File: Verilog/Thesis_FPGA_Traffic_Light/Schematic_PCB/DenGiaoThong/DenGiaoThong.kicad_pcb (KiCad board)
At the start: 2 copper layers, 33 parts, among them J1 Conn_01x10_Male, Q1 2SC1815, Q2 2SC1815, Q3 2SC1815, Q4 2SC1815, Q5 2SC1815, Q6 2SC1815, Q7 2SC1815, Q8 2SC1815

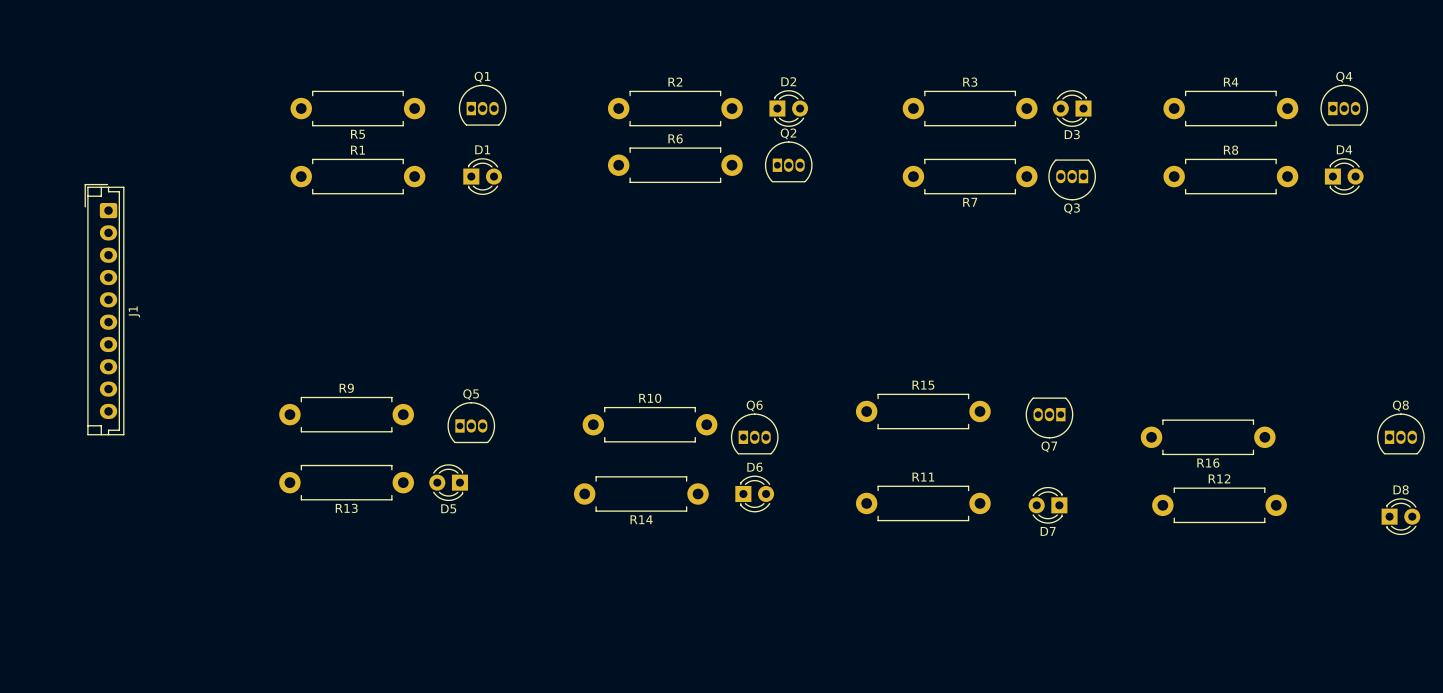
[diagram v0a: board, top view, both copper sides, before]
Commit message: update test git ignore
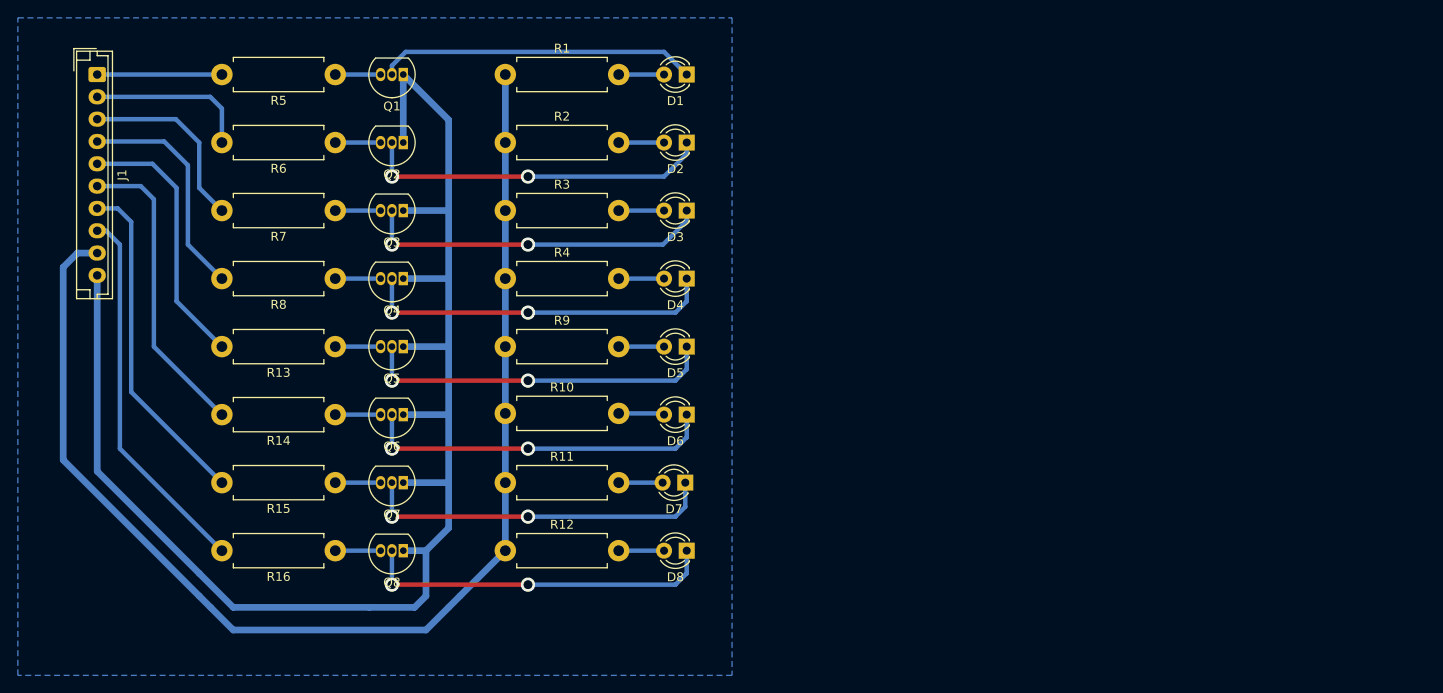
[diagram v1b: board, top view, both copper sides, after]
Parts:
- moved Q8 111.2 mm to (68.6, 80.0), turned to 180 degrees
- moved Q4 105.9 mm to (68.6, 49.5), turned to 180 degrees
- moved R16 104.9 mm to (61.0, 80.0)
- moved R8 94.7 mm to (61.0, 49.5), turned to 180 degrees
- moved D8 78.8 mm to (100.3, 80.0), turned to 180 degrees
- moved R7 77.6 mm to (61.0, 41.9)
- moved R4 77.3 mm to (80.0, 49.5)
- moved Q3 76.3 mm to (68.6, 41.9)
- moved Q7 74.1 mm to (68.6, 72.4)
- moved R12 73.8 mm to (80.0, 80.0)
- moved D4 73.3 mm to (100.3, 49.5), turned to 180 degrees
- moved R15 60.1 mm to (61.0, 72.4), turned to 180 degrees
- moved R3 47.1 mm to (80.0, 41.9)
- moved D3 45.9 mm to (100.3, 41.9)
- moved D7 42.0 mm to (100.2, 72.4)
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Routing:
- net GNDREF: track 0.00 -> 162.2 mm
- net /5V: track 0.00 -> 140.5 mm
- net /SB_PL: track 0.00 -> 42.2 mm
- net Net-(D6-Pad1): track 0.00 -> 39.9 mm, vias 0 -> 2
- net Net-(D5-Pad1): track 0.00 -> 39.9 mm, vias 0 -> 2
- net Net-(D4-Pad1): track 0.00 -> 39.9 mm, vias 0 -> 2
- net Net-(D8-Pad1): track 0.00 -> 39.9 mm, vias 0 -> 2
- net Net-(D7-Pad1): track 0.00 -> 39.8 mm, vias 0 -> 2
- net Net-(D2-Pad1): track 0.00 -> 39.2 mm, vias 0 -> 2
- net Net-(D3-Pad1): track 0.00 -> 39.1 mm, vias 0 -> 2
- net /SB_0: track 0.00 -> 37.9 mm
- net Net-(D1-Pad1): track 0.00 -> 35.7 mm
- net /SB_1: track 0.00 -> 34.2 mm
- net /SB_2: track 0.00 -> 30.1 mm
- net /SA_PL: track 0.00 -> 25.5 mm
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- added copper zone on B.Cu, net GNDREF
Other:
- net class Default: trace_width 0.25 -> 0.5; via_dia 0.8 -> 2; via_drill 0.4 -> 1
- net class Power added: clearance 0.2, trace_width 0.75, via_dia 2, via_drill 1
- net class Signal added: clearance 0.2, trace_width 0.5, via_dia 1.6, via_drill 1

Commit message: update the PCB file and generate PDF
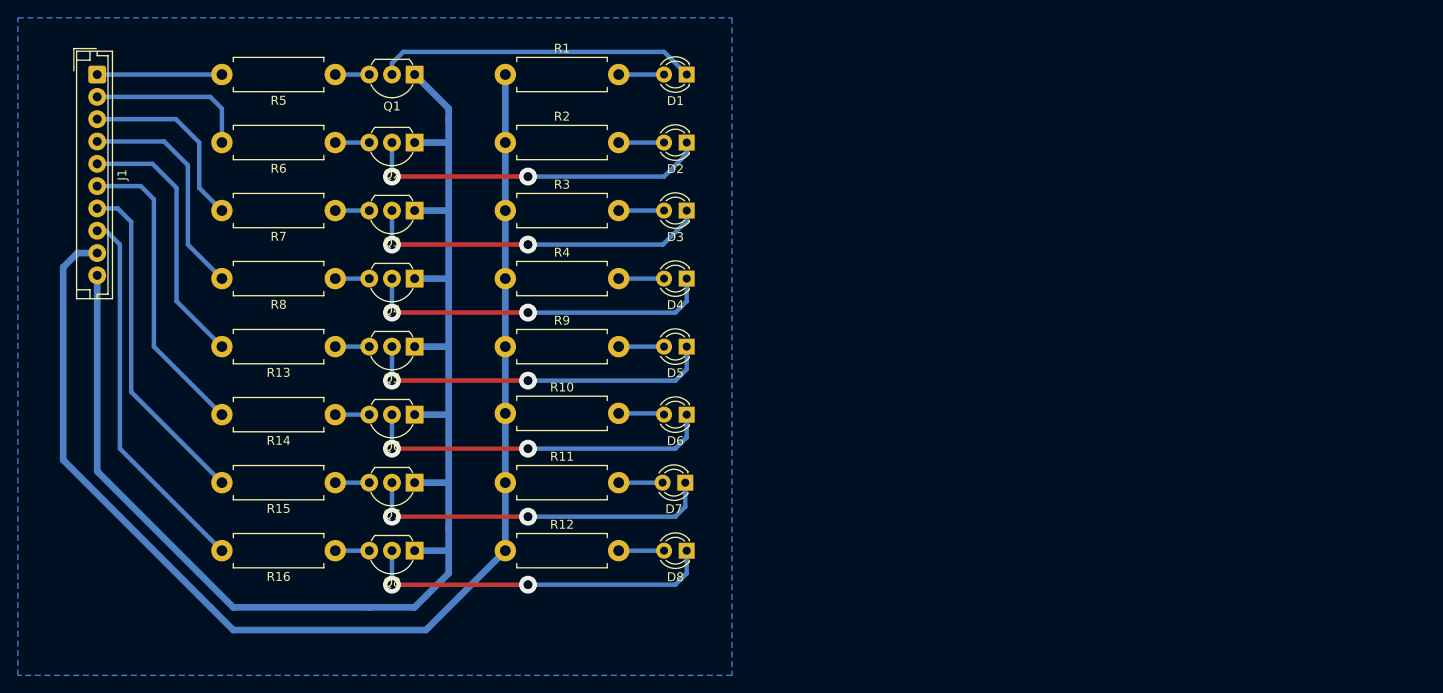
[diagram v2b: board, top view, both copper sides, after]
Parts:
- Q1, Q2, Q3, Q4, Q5, Q6, Q7, Q8: footprint Package_TO_SOT_THT:TO-92_Inline -> Package_TO_SOT_THT:TO-92L_Inline_Wide
- moved Q1 1.27 mm to (69.8, 26.7)
- moved Q2 1.27 mm to (69.8, 34.3)
- moved Q3 1.27 mm to (69.8, 41.9)
- moved Q4 1.27 mm to (69.8, 49.5)
- moved Q5 1.27 mm to (69.8, 57.1)
- moved Q6 1.27 mm to (69.8, 64.8)
- moved Q7 1.27 mm to (69.8, 72.4)
- moved Q8 1.27 mm to (69.8, 80.0)
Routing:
- net GNDREF: track 162.2 -> 153.3 mm
- net Net-(Q8-Pad3): track 5.08 -> 3.81 mm
- net Net-(Q7-Pad3): track 5.08 -> 3.81 mm
- net Net-(Q6-Pad3): track 5.08 -> 3.81 mm
- net Net-(Q5-Pad3): track 5.08 -> 3.81 mm
- net Net-(Q4-Pad3): track 5.08 -> 3.81 mm
- net Net-(Q3-Pad3): track 5.08 -> 3.81 mm
- net Net-(Q2-Pad3): track 5.08 -> 3.81 mm
- net Net-(Q1-Pad3): track 5.08 -> 3.81 mm
